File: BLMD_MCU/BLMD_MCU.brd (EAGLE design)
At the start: 30 x 58.5 mm, 2 parts

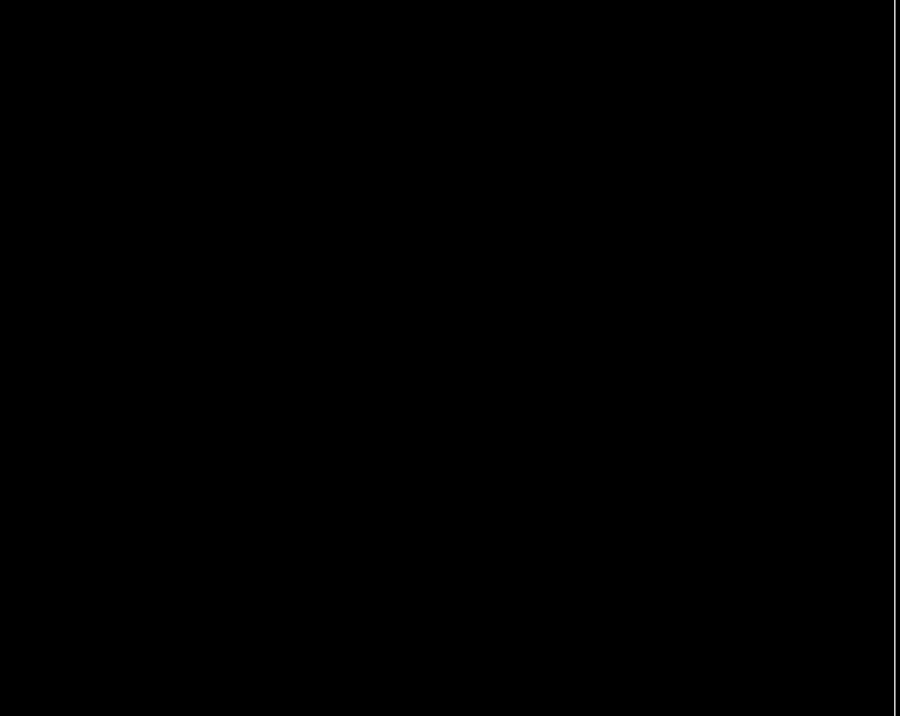
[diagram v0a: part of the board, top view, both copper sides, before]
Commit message: UVW結線のふっとぷりんと追加、新ガーバーファイル追加
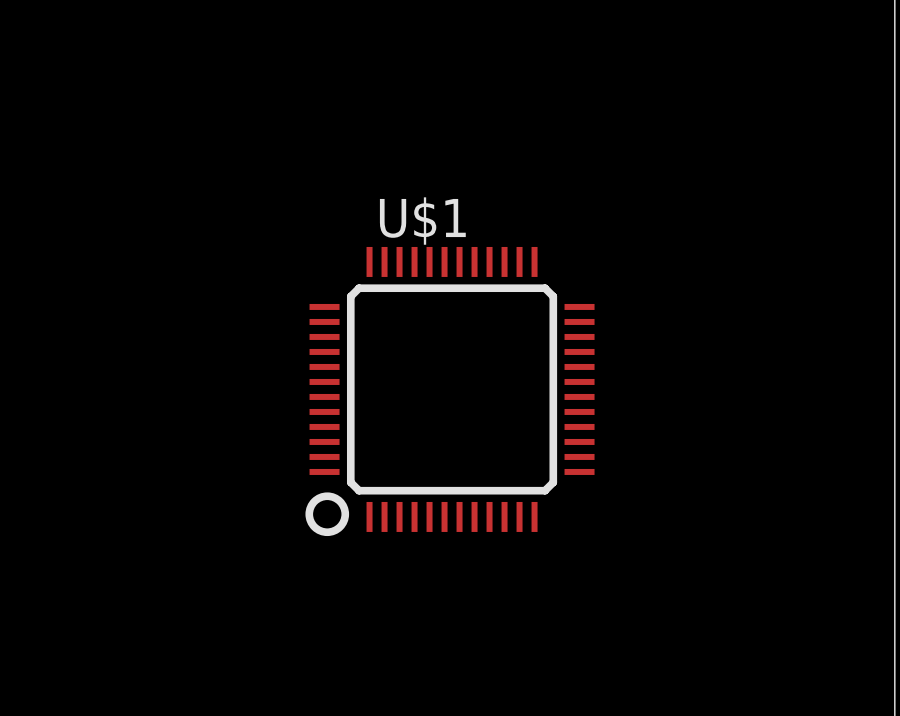
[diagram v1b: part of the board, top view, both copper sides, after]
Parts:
- added U$1: PIC32MK0512MCJ048, user_ic:LQFP48PIN
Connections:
- new net AGND: CON2.P$5, CON2.P$7
- new net AHI: CON1.P$2
- new net ALO: CON1.P$1
- new net AVCC: CON2.P$4
- new net BHI: CON1.P$4
- new net BLO: CON1.P$3
- new net CHI: CON1.P$6
- new net CLO: CON1.P$5
- new net GND: CON1.P$7, CON1.P$8, CON2.P$3
- new net MD_FAULT: CON2.P$2
- new net U_CURRENT: CON2.P$6
- new net VCC: CON2.P$1
- new net W_CURRENT: CON2.P$8
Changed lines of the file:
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@@
 <element name="CON1" library="user_conector" package="JQ_S8P" value="" x="29.06" y="0.35" locked="yes" smashed="yes" rot="MR0"/>
 <element name="CON2" library="user_conector" package="JQ_S8P" value="" x="29.06" y="51.15" locked="yes" smashed="yes" rot="MR0"/>
+<element name="U$1" library="user_ic" package="LQFP48PIN" value="PIC32MK0512MCJ048" x="15.24" y="29.21" smashed="yes">
+<attribute name="NAME" x="12.7" y="34.29" size="1.27" layer="25"/>
+<attribute name="VALUE" x="12.7" y="22.86" size="1.27" layer="27"/>
+</element>
 </elements>
 <signals>
+<signal name="ALO">
+<contactref element="CON1" pad="P$1"/>
+</signal>
+<signal name="AHI">
+<contactref element="CON1" pad="P$2"/>
+</signal>
+<signal name="BLO">
+<contactref element="CON1" pad="P$3"/>
+</signal>
+<signal name="BHI">
+<contactref element="CON1" pad="P$4"/>
+</signal>
+<signal name="CLO">
+<contactref element="CON1" pad="P$5"/>
+</signal>
+<signal name="CHI">
+<contactref element="CON1" pad="P$6"/>
+</signal>
+<signal name="VCC">
+<contactref element="CON2" pad="P$1"/>
+</signal>
+<signal name="MD_FAULT">
+<contactref element="CON2" pad="P$2"/>
+</signal>
+<signal name="GND">
+<contactref element="CON2" pad="P$3"/>
+<contactref element="CON1" pad="P$7"/>
+<contactref element="CON1" pad="P$8"/>
+<wire x1="11.56" y1="3.05" x2="21.56" y2="53.85" width="0" layer="19" extent="1-1"/>
+<wire x1="9.06" y1="3.05" x2="11.56" y2="3.05" width="0" layer="19" extent="1-1"/>
+</signal>
+<signal name="AVCC">
+<contactref element="CON2" pad="P$4"/>
+</signal>
+<signal name="AGND">
+<contactref element="CON2" pad="P$5"/>
+<contactref element="CON2" pad="P$7"/>
+<wire x1="11.56" y1="53.85" x2="16.56" y2="53.85" width="0" layer="19" extent="1-1"/>
+</signal>
+<signal name="U_CURRENT">
+<contactref element="CON2" pad="P$6"/>
+</signal>
+<signal name="W_CURRENT">
+<contactref element="CON2" pad="P$8"/>
+</signal>
 </signals>
 <mfgpreviewcolors>

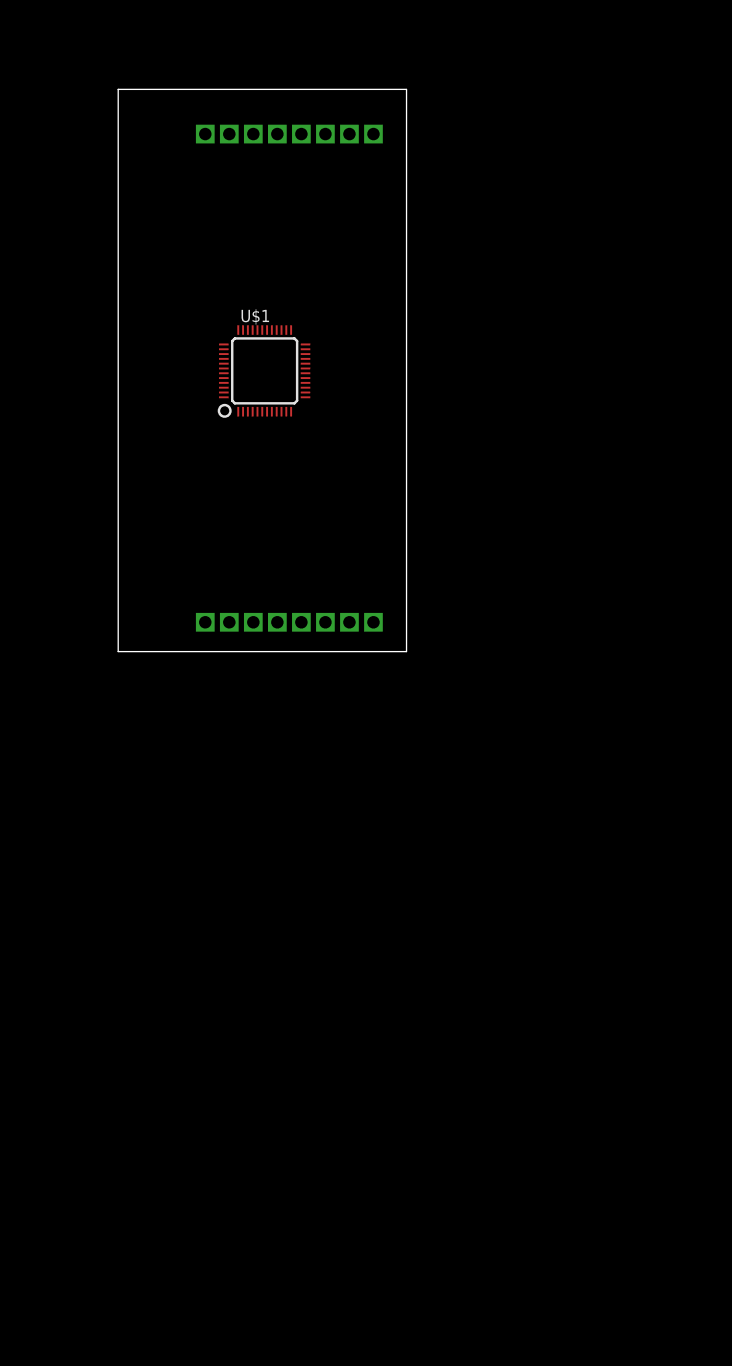
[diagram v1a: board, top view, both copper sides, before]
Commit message: MCU側回路図を作成
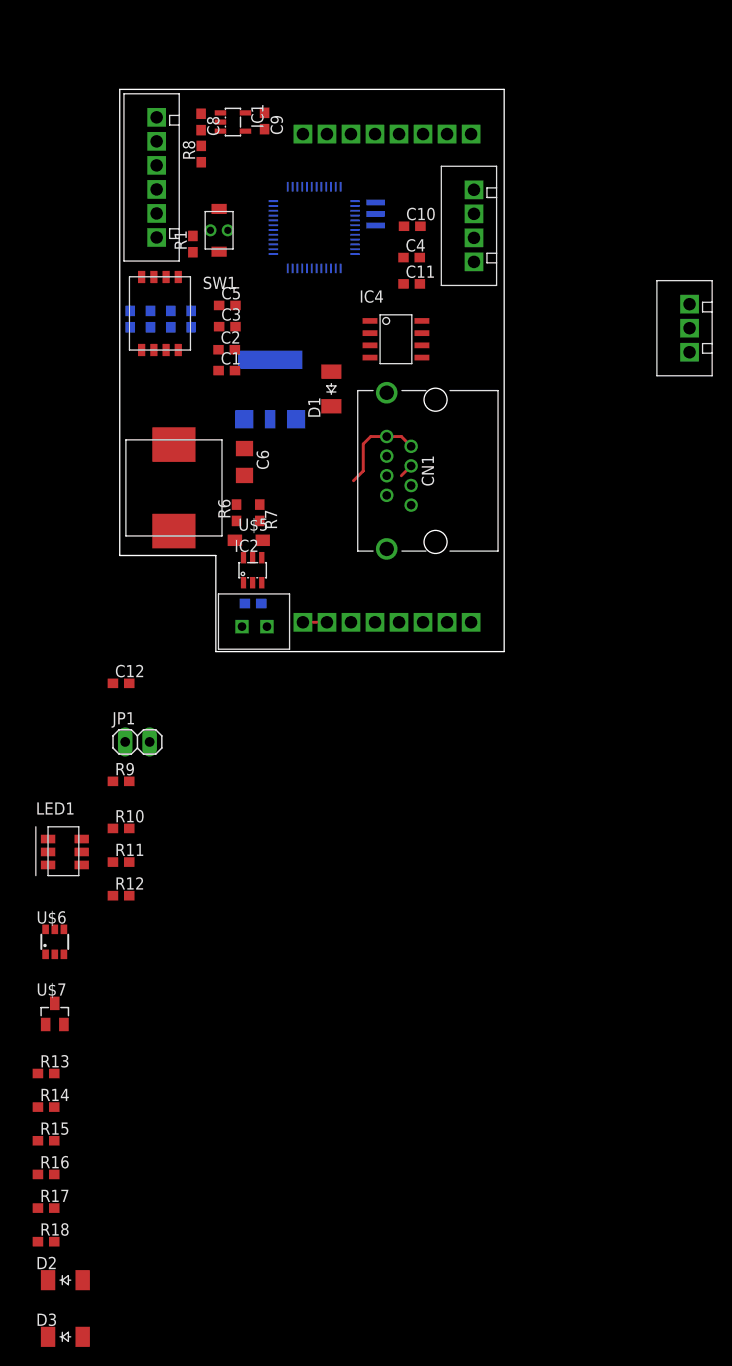
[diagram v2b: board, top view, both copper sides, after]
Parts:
- added C1, C12, C2, C4, C5: 0.1u, rcl:C1608
- added C10: 2.2u, rcl:C1608
- added C11, C8, C9: 1u, rcl:C1608
- added C3: (no value), rcl:C1608
- added C6: 100u, rcl:C3216
- added C7: 10u, rcl:C1608
- added CN1: 7810-8P8C, user_conector:78108P8C
- added CON3: (no value), user_conector:XH_4P
- added CON4: (no value), user_conector:XH_6P
- added CON5: (no value), user_conector:XH_3P
- added D1, D2, D3: SBR2U30P1, user_diode:SOD_123
- added IC1: ADP151AUJZ, user_ic:SOT23-5
- added IC2: (no value), user_ic:SOT23-6
- added IC3: AZ1117CH, user_ic:SOT223-W
- added IC4: (no value), user_ic:SOIC8
- added JP1: (no value), pinhead:1X02
- added L1: 47u, user_rcl:SMD_INDUCTOR
- added LED1: RGB_LED, user_leds:RGB_LED
- added OSC1: 20MHz, user_osc:CSTNE#
- added R1, R6: 10k, user_rcl:1608
- added R10, R11, R12, R16, R17, R18, R2, R3, R4, R5: (no value), user_rcl:1608
- added R13, R14, R15: 47k, user_rcl:1608
- added R7: 3.3k, user_rcl:1608
- added R8: 0, user_rcl:1608
- added R9: 120, user_rcl:1608
- added SW1: (no value), user_swich:DIPSW4
- added U$2: TAKUTOSUITTI2, user_swich:TAKUTOSUITTI2
- added U$4: XH_2P, user_conector:XH_2P
- added U$5: CUHS20S30, user_diode:SOD323-W
- added U$6: FDC6305, user_tr_fet_igbt:SSOT6
- added U$7: SOT23_NFET, user_tr_fet_igbt:SOT23
- moved U$1 15.8 mm to (20.4, 44.1), flipped to the bottom, turned to 90 degrees
- moved CON1 10.2 mm to (39.2, 0.35)
- moved CON2 10.2 mm to (39.2, 51.1)
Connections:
- new net +5V: C11.1, C12.1, C6.1, C8.1, D1.K, IC1.1, IC1.3, IC3.3, IC4.P$3, L1.P$2, R6.2
- new net CANH: CN1.6, CON5.P$1, IC4.P$7, JP1.1
- new net CANL: CN1.3, CON5.P$2, IC4.P$6, R9.1
- new net CAN_RX: IC4.P$4, U$1.PIN25
- new net CAN_TX: IC4.P$1, U$1.PIN24
- new net FF1_LED: R14.1, U$1.PIN35, U$6.1
- new net FF2_LED: R15.1, U$1.PIN36, U$6.3
- new net HOME1: U$1.PIN19
- new net ID_1: R2.2, SW1.P$1, U$1.PIN1
- new net ID_2: R3.2, SW1.P$2, U$1.PIN48
- new net ID_3: R4.2, SW1.P$3, U$1.PIN47
- new net ID_4: R5.2, SW1.P$4, U$1.PIN46
- new net INDX1: U$1.PIN18
- new net MCLR: C1.1, CON4.P$1, R1.1, U$1.PIN4, U$2.P$1
- new net N$1: R12.2, U$1.PIN8
- new net N$10: IC2.3, R6.1, R7.2
- new net N$11: LED1.R_A, R16.2
- new net N$12: LED1.B_K, U$7.PIN3
- new net N$13: CON3.P$1, D1.A
- new net N$14: LED1.G_K, U$6.6
- new net N$15: LED1.R_K, U$6.4
- new net N$16: D2.A, U$4.P$1
- new net N$17: R13.1, R14.2, R15.2, U$7.PIN2
- new net N$18: CN1.4, D3.A
- new net N$2: R11.2, U$1.PIN10
- new net N$3: LED1.B_A, R18.2
- new net N$4: R10.2, U$1.PIN12
- new net N$5: OSC1.P$3, U$1.PIN27
- new net N$6: OSC1.P$1, U$1.PIN28
- new net N$7: LED1.G_A, R17.2
- new net N$8: JP1.2, R9.2
- new net N$9: IC2.6, L1.P$1, U$5.C
- new net PGC: CON4.P$5, U$1.PIN13
- new net PGD: CON4.P$4, U$1.PIN14
- new net QEA1: U$1.PIN17
- new net QEB1: U$1.PIN23
- new net QEICMP1: U$1.PIN3
- new net STAT_LED: R13.2, U$1.PIN31, U$7.PIN1
- new net UART_RX: CON3.P$2, U$1.PIN32
- new net UART_TX: CON3.P$3, U$1.PIN34
- new net V+: C7.1, CN1.5, D2.K, D3.K, IC2.4, IC2.5
- net AGND: now also C8.2, C9.2, IC1.2, R10.1, R11.1, R12.1, R8.2, U$1.PIN16
- net AHI: now also U$1.PIN38
- net ALO: now also U$1.PIN39
- net AVCC: now also C9.1, IC1.5, U$1.PIN15
- net BHI: now also U$1.PIN40
- net BLO: now also U$1.PIN41
- net CHI: now also U$1.PIN44
- net CLO: now also U$1.PIN45
- net GND: now also C1.2, C10.2, C11.2, C12.2, C2.2, C3.2, C4.2, C5.2, C6.2, C7.2, CN1.7, CN1.8, CON3.P$4, CON4.P$3, CON5.P$3, IC2.2, IC3.1, IC4.P$2, IC4.P$8, OSC1.P$2, R2.1, R3.1, R4.1, R5.1, R7.1, R8.1, U$1.PIN21, U$1.PIN29, U$1.PIN42, U$1.PIN5, U$2.P$2, U$4.P$2, U$5.A
- net MD_FAULT: now also U$1.PIN30
- net U_CURRENT: now also U$1.PIN11
- net VCC: now also C10.1, C2.1, C3.1, C4.1, C5.1, CON4.P$2, IC3.2, IC3.4, IC4.P$5, R1.2, R16.1, R17.1, R18.1, SW1.P$5, SW1.P$6, SW1.P$7, SW1.P$8, U$1.PIN22, U$1.PIN26, U$1.PIN43, U$1.PIN6
- net W_CURRENT: now also U$1.PIN9
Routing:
- net GND: track 0.00 -> 12.5 mm
- net V+: track 0.00 -> 1.44 mm
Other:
- board size 30 x 58.5 mm -> 40 x 58.5 mm

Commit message: 基板完成　ガーバーファイル追加
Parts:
- moved R18 96.8 mm to (2.40, 34.9), flipped to the bottom, turned to 180 degrees
- moved R17 91.1 mm to (2.40, 32.7), flipped to the bottom, turned to 180 degrees
- moved D3 90.4 mm to (25.2, 13.7), flipped to the bottom, turned to 90 degrees
- moved R15 89.4 mm to (5.20, 37.6), turned to 270 degrees
- moved R14 86.3 mm to (7.30, 37.6), turned to 270 degrees
- moved R16 85.5 mm to (2.40, 30.5), flipped to the bottom, turned to 180 degrees
- moved R13 85.4 mm to (2.30, 40.9), flipped to the bottom, turned to 180 degrees
- moved U$7 76.3 mm to (2.30, 38.1), turned to 180 degrees
- moved D2 75.4 mm to (13.8, 7.50), turned to 180 degrees
- moved R12 74.7 mm to (19.8, 46.7), flipped to the bottom, turned to 270 degrees
- moved R11 71.9 mm to (21.9, 46.7), flipped to the bottom, turned to 270 degrees
- moved R10 69.3 mm to (24.0, 46.7), flipped to the bottom, turned to 270 degrees
- moved U$6 69.0 mm to (6.40, 37.6), flipped to the bottom, turned to 270 degrees
- moved LED1 53.2 mm to (6.90, 31.8), turned to 180 degrees
- moved R9 49.9 mm to (26.2, 29.1)
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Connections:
- removed net N$17: R13.1, R14.2, R15.2, U$7.PIN2
- net GND: now also R13.1, R14.2, R15.2, U$7.PIN2
- net N$18: now also CN1.5
- net V+: no longer CN1.5
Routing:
- net VCC: track 0.00 -> 147.9 mm, vias 0 -> 6
- net +5V: track 0.00 -> 99.0 mm, vias 0 -> 6
- net GND: track 12.5 -> 94.7 mm, vias 0 -> 46
- net CHI: track 0.00 -> 70.5 mm, vias 0 -> 1
- net CLO: track 0.00 -> 68.1 mm
- net BHI: track 0.00 -> 66.3 mm, vias 0 -> 1
- net BLO: track 0.00 -> 64.0 mm
- net AHI: track 0.00 -> 61.4 mm, vias 0 -> 1
- net ALO: track 0.00 -> 58.8 mm
- net UART_TX: track 0.00 -> 50.5 mm, vias 0 -> 2
- net MD_FAULT: track 0.00 -> 44.2 mm
- net N$13: track 0.00 -> 43.6 mm, vias 0 -> 2
- net UART_RX: track 0.00 -> 43.2 mm, vias 0 -> 2
- net CANL: track 0.00 -> 42.1 mm
- net CANH: track 0.00 -> 40.6 mm
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- added copper zone on layer 1, net +5V
- added copper zone on layer 16, net +5V
- added copper zone on layer 1, net AGND
- added copper zone on layer 16, net AGND
- added copper zone on layer 1, net GND
- added copper zone on layer 16, net GND
- added copper zone on layer 1, net N$16
- added copper zone on layer 16, net N$18
- added copper zone on layer 1, net N$9
- added copper zone on layer 1, net V+
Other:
- board text added: "+"
- board text added: "0.Hayate"
- board text added: "1"
- board text added: "4"
- board text added: "5"
- board text added: "C"
- board text added: "D"
- board text added: "FF1"
- board text added: "FF2"
- board text added: "ForCoRE"
- board text added: "G"
- board text added: "H"
- board text added: "ID_Select"
- board text added: "L"
- board text added: "MotaCon_MCU"
- board text added: "R"
- board text added: "Reset"
- board text added: "Stat"
- board text added: "T"
- board text added: "V"

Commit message: ガーバーファイル追加
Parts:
- U$7: value SOT23_NFET -> AO3400A
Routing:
- net AGND: track 39.8 -> 28.7 mm
- net GND: track 94.7 -> 87.2 mm
- net N$18: track 5.60 -> 4.16 mm
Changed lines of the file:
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@@
 <attribute name="NAME" x="8.553" y="39.126" size="1.27" layer="26" rot="MR180"/>
 </element>
-<element name="U$7" library="user_tr_fet_igbt" package="SOT23" value="SOT23_NFET" x="2.3" y="38.1" smashed="yes" rot="R180">
+<element name="U$7" library="user_tr_fet_igbt" package="SOT23" value="AO3400A" x="2.3" y="38.1" smashed="yes" rot="R180">
 <attribute name="NAME" x="0.635" y="35.955" size="1.27" layer="25" rot="R270"/>
 </element>
@@
 <wire x1="15.48" y1="3.52" x2="15.48" y2="2.6" width="0.3048" layer="16"/>
 <wire x1="14.88" y1="4.12" x2="15.48" y2="3.52" width="0.3048" layer="16"/>
-<wire x1="15.04" y1="11.58" x2="15.97" y2="12.51" width="0.3048" layer="1"/>
-<wire x1="15.97" y1="12.51" x2="17.07" y2="12.51" width="0.3048" layer="1"/>
 <wire x1="13.14" y1="18.33" x2="13.14" y2="17.13" width="0.3048" layer="1"/>
 <wire x1="14.23" y1="16.04" x2="13.14" y2="17.13" width="0.3048" layer="1"/>
@@
 <wire x1="19.51" y1="19.56" x2="17.06" y2="19.56" width="0.3048" layer="1"/>
 <wire x1="13.14" y1="18.33" x2="15.83" y2="18.33" width="0.3048" layer="1"/>
-<wire x1="15.83" y1="18.33" x2="17.06" y2="19.56" width="0.3048" layer="1"/>
 <wire x1="27.84" y1="19.58" x2="19.53" y2="19.58" width="0.3048" layer="1"/>
 <wire x1="19.53" y1="19.58" x2="19.51" y2="19.56" width="0.3048" layer="1"/>
 <wire x1="14.23" y1="15.3" x2="15.4" y2="15.3" width="0.3048" layer="1"/>
-<wire x1="15.97" y1="14.73" x2="15.97" y2="12.51" width="0.3048" layer="1"/>
 <wire x1="15.4" y1="15.3" x2="15.97" y2="14.73" width="0.3048" layer="1"/>
 <wire x1="21.71" y1="14.97" x2="22.1" y2="15.36" width="0.3048" layer="16"/>
@@
 <wire x1="5.2" y1="36.75" x2="7.3" y2="36.75" width="0.3048" layer="1"/>
 <wire x1="5.2" y1="36.75" x2="4.18105" y2="36.75" width="0.3048" layer="1"/>
-<wire x1="2.12375" y1="38.1952" x2="1.35" y2="38.96895" width="0.3048" layer="1"/>
 <wire x1="1.35" y1="39.2" x2="1.35" y2="38.96895" width="0.3048" layer="1"/>
 <wire x1="2.73585" y1="38.1952" x2="2.12375" y2="38.1952" width="0.3048" layer="1"/>
@@
 <contactref element="R11" pad="1"/>
 <contactref element="R10" pad="1"/>
-<wire x1="19.8" y1="47.55" x2="20.4428" y2="48.1928" width="0.3048" layer="16"/>
-<wire x1="20.4428" y1="49.21061875" x2="18.7628" y2="50.89061875" width="0.3048" layer="16"/>
 <wire x1="18.7628" y1="50.89061875" x2="18.7628" y2="51.6372" width="0.3048" layer="16"/>
 <wire x1="17.9402" y1="52.4598" x2="17.9402" y2="55.0402" width="0.3048" layer="16"/>
@@
 <wire x1="21.72" y1="55.68" x2="21.72" y2="54" width="0.3048" layer="16"/>
 <wire x1="21.72" y1="54" x2="21.72" y2="53.85" width="0.3048" layer="16"/>
-<wire x1="20.4428" y1="48.1928" x2="20.4428" y2="49.21061875" width="0.3048" layer="16"/>
 <wire x1="18.7628" y1="51.6372" x2="17.9402" y2="52.4598" width="0.3048" layer="16"/>
 <wire x1="21.9" y1="47.55" x2="21.9" y2="53.82" width="0.3048" layer="16"/>
 <wire x1="21.9" y1="53.82" x2="21.72" y2="54" width="0.3048" layer="16"/>
-<wire x1="24" y1="47.55" x2="23.273290625" y2="48.276709375" width="0.3048" layer="16"/>
-<wire x1="23.273290625" y1="48.276709375" x2="23.273290625" y2="49.226709375" width="0.3048" layer="16"/>
-<wire x1="23.273290625" y1="49.226709375" x2="24.6772" y2="50.63061875" width="0.3048" layer="16"/>
-<wire x1="24.6772" y1="51.8072" x2="26.72" y2="53.85" width="0.3048" layer="16"/>
 <wire x1="24.6772" y1="50.63061875" x2="24.6772" y2="51.8072" width="0.3048" layer="16"/>
 <wire x1="26.72" y1="53.85" x2="26.72" y2="55.28" width="0.3048" layer="16"/>
@@
 <contactref element="CN1" pad="4"/>
 <contactref element="CN1" pad="5"/>
-<wire x1="30.38" y1="16.52" x2="29.36" y2="15.5" width="0.3048" layer="16"/>
 <wire x1="29.36" y1="15.5" x2="27.84" y2="15.5" width="0.3048" layer="16"/>
 <wire x1="27.84" y1="15.5" x2="25.2" y2="15.5" width="0.3048" layer="16"/>
